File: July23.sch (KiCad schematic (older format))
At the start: 42 parts, among them P1 12v In, P2 HeatOut, P3 LED, P4 Temp1, P5 Temp2, P6 Temp3, P7 ExtPwr, Q16 Q_NMOS_GSD, Q17 Q_NMOS_GSD, U1 Teensy_3.1, U2 LM358, U3 CD74HC4067, U4 MC78M05CDT, U5 NCR405U

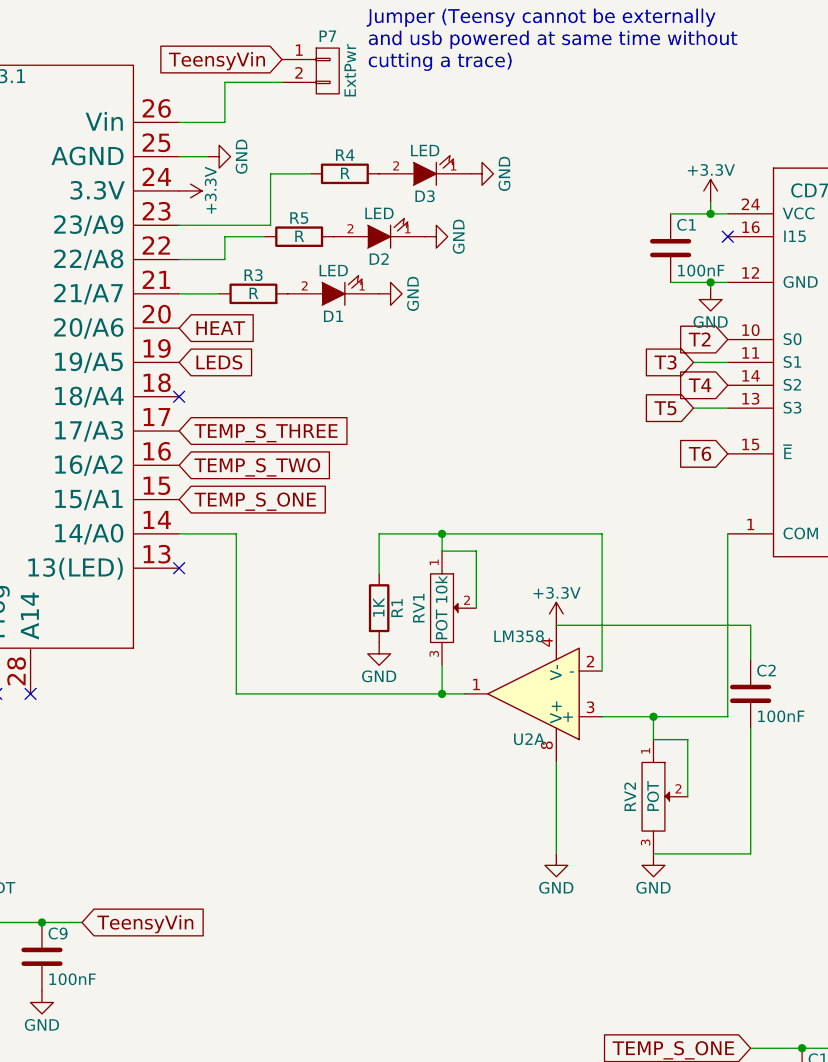
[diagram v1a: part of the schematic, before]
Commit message: OpAmp circuit needs checking
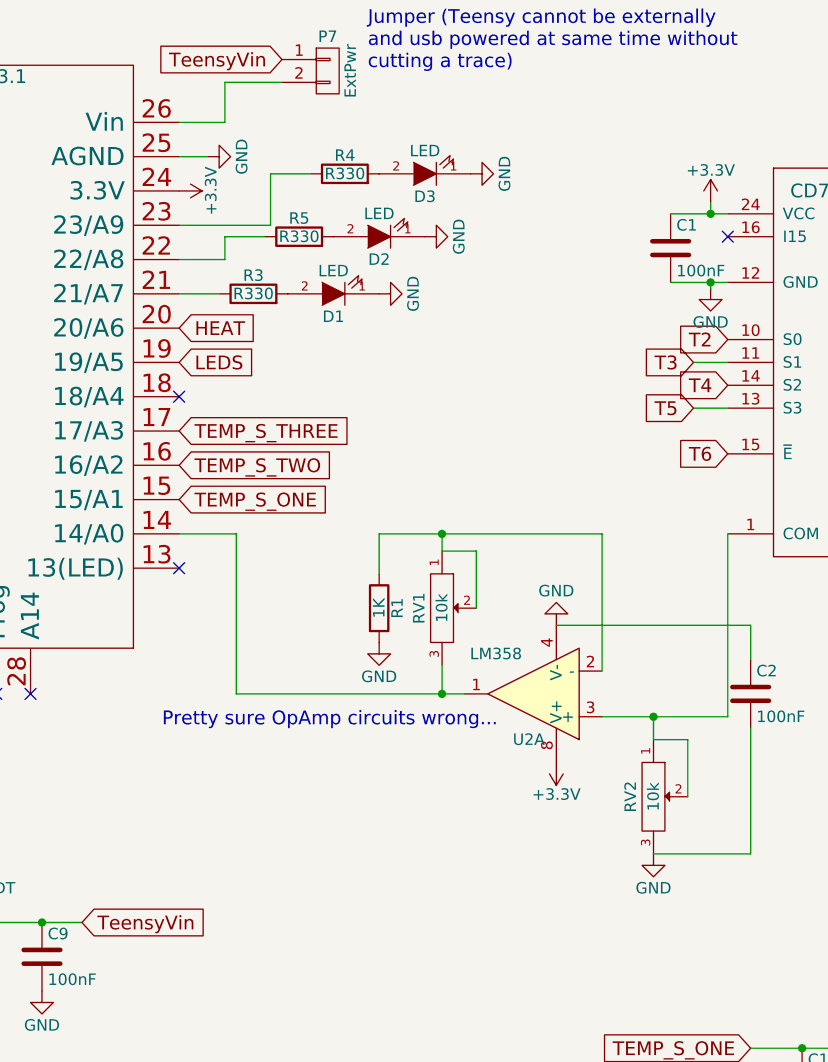
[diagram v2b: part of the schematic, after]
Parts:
- R3, R4, R5: value R -> R330
- RV1: value POT 10k -> 10k
- RV2: value POT -> 10k
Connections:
- net +3V3: now also U2.8 (V+); no longer C2.1, U2.4 (V-)
- net GND: now also C2.1, U2.4 (V-); no longer U2.8 (V+)
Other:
- note added: "Pretty sure OpAmp circuits wrong..."
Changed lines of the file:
@@
 P 4575 3650
 F 0 "U2" H 4525 3850 50  0000 L CNN
-F 1 "LM358" H 4525 3400 50  0000 L CNN
+F 1 "LM358" H 4625 3475 50  0000 L CNN
 F 2 "Housings_DIP:DIP-8_W7.62mm" H 4575 3650 50  0001 C CNN
 F 3 "" H 4575 3650 50  0000 C CNN
@@
 P 5100 4100
 F 0 "RV2" H 5100 4000 50  0000 C CNN
-F 1 "POT" H 5100 4100 50  0000 C CNN
+F 1 "10k" H 5100 4100 50  0000 C CNN
 F 2 "Potentiometers:Potentiometer_Trimmer-Suntan-TSR-3386P" H 5100 4100 50  0001 C CNN
 F 3 "" H 5100 4100 50  0000 C CNN
@@
 P 4175 3275
 F 0 "RV1" H 4175 3175 50  0000 C CNN
-F 1 "POT 10k" H 4175 3275 50  0000 C CNN
+F 1 "10k" H 4175 3275 50  0000 C CNN
 F 2 "Potentiometers:Potentiometer_Trimmer-Suntan-TSR-3386P" H 4175 3275 50  0001 C CNN
 F 3 "" H 4175 3275 50  0000 C CNN
@@
 L +3.3V #PWR08
 U 1 1 56C888B3
-P 4675 3350
-F 0 "#PWR08" H 4675 3200 50  0001 C CNN
-F 1 "+3.3V" H 4675 3490 50  0000 C CNN
-F 2 "" H 4675 3350 50  0000 C CNN
-F 3 "" H 4675 3350 50  0000 C CNN
-	1    4675 3350
-	1    0    0    -1
+P 4675 3950
+F 0 "#PWR08" H 4675 3800 50  0001 C CNN
+F 1 "+3.3V" H 4675 4090 50  0000 C CNN
+F 2 "" H 4675 3950 50  0000 C CNN
+F 3 "" H 4675 3950 50  0000 C CNN
+	1    4675 3950
+	-1   0    0    1
 $EndComp
 $Comp
@@
 P 3350 1900
 F 0 "R3" V 3430 1900 50  0000 C CNN
-F 1 "R" V 3350 1900 50  0000 C CNN
+F 1 "R330" V 3350 1900 50  0000 C CNN
 F 2 "Resistors_SMD:R_0805_HandSoldering" V 3280 1900 50  0001 C CNN
 F 3 "" H 3350 1900 50  0000 C CNN
@@
 P 3750 1375
 F 0 "R4" V 3830 1375 50  0000 C CNN
-F 1 "R" V 3750 1375 50  0000 C CNN
+F 1 "R330" V 3750 1375 50  0000 C CNN
 F 2 "Resistors_SMD:R_0805_HandSoldering" V 3680 1375 50  0001 C CNN
 F 3 "" H 3750 1375 50  0000 C CNN
@@
 P 3550 1650
 F 0 "R5" V 3630 1650 50  0000 C CNN
-F 1 "R" V 3550 1650 50  0000 C CNN
+F 1 "R330" V 3550 1650 50  0000 C CNN
 F 2 "Resistors_SMD:R_0805_HandSoldering" V 3480 1650 50  0001 C CNN
 F 3 "" H 3550 1650 50  0000 C CNN
@@
 L GND #PWR015
 U 1 1 56E2450E
-P 4675 4350
-F 0 "#PWR015" H 4675 4100 50  0001 C CNN
-F 1 "GND" H 4675 4200 50  0000 C CNN
-F 2 "" H 4675 4350 50  0000 C CNN
-F 3 "" H 4675 4350 50  0000 C CNN
-	1    4675 4350
-	1    0    0    -1
+P 4675 3350
+F 0 "#PWR015" H 4675 3100 50  0001 C CNN
+F 1 "GND" H 4675 3200 50  0000 C CNN
+F 2 "" H 4675 3350 50  0000 C CNN
+F 3 "" H 4675 3350 50  0000 C CNN
+	1    4675 3350
+	-1   0    0    1
 $EndComp
 $Comp
@@
 	5100 3850 5250 3850
 Wire Wire Line
-	4675 4350 4675 3950
-Wire Wire Line
 	4175 3025 4325 3025
 Wire Wire Line
@@
 	1200 4375 1200 4650
 Connection ~ 1200 4650
+Text Notes 2950 3800 0    60   ~ 0
+Pretty sure OpAmp circuits wrong...
 $EndSCHEMATC

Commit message: opamp flipped for clarity
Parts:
- RV1, RV2: symbol POT -> POT-RESCUE-July23
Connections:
- net labels added: Amp+, Amp-, Amp_Out
- wire segments 96 -> 94
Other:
- note removed: "Pretty sure OpAmp circuits wrong..."
- moved on the sheet: C2, R1
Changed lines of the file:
@@
 EESchema Schematic File Version 2
+LIBS:July23-rescue
 LIBS:power
 LIBS:device
@@
 F 3 "" H 4575 3650 50  0000 C CNN
 	1    4575 3650
-	-1   0    0    1
-$EndComp
-$Comp
-L POT RV2
+	-1   0    0    -1
+$EndComp
+$Comp
+L POT-RESCUE-July23 RV2
 U 1 1 56B985A4
-P 5100 4100
-F 0 "RV2" H 5100 4000 50  0000 C CNN
-F 1 "10k" H 5100 4100 50  0000 C CNN
-F 2 "Potentiometers:Potentiometer_Trimmer-Suntan-TSR-3386P" H 5100 4100 50  0001 C CNN
-F 3 "" H 5100 4100 50  0000 C CNN
-	1    5100 4100
+P 5425 4100
+F 0 "RV2" H 5425 4000 50  0000 C CNN
+F 1 "10k" H 5425 4100 50  0000 C CNN
+F 2 "Potentiometers:Potentiometer_Trimmer-Suntan-TSR-3386P" H 5425 4100 50  0001 C CNN
+F 3 "" H 5425 4100 50  0000 C CNN
+	1    5425 4100
 	0    1    1    0
 $EndComp
 $Comp
-L POT RV1
+L POT-RESCUE-July23 RV1
 U 1 1 56B99053
-P 4175 3275
-F 0 "RV1" H 4175 3175 50  0000 C CNN
-F 1 "10k" H 4175 3275 50  0000 C CNN
-F 2 "Potentiometers:Potentiometer_Trimmer-Suntan-TSR-3386P" H 4175 3275 50  0001 C CNN
-F 3 "" H 4175 3275 50  0000 C CNN
-	1    4175 3275
-	0    1    1    0
+P 4175 4025
+F 0 "RV1" H 4175 3925 50  0000 C CNN
+F 1 "10k" H 4175 4025 50  0000 C CNN
+F 2 "Potentiometers:Potentiometer_Trimmer-Suntan-TSR-3386P" H 4175 4025 50  0001 C CNN
+F 3 "" H 4175 4025 50  0000 C CNN
+	1    4175 4025
+	0    1    -1   0
 $EndComp
 $Comp
 L R R1
 U 1 1 56B99A73
-P 3900 3275
-F 0 "R1" V 3980 3275 50  0000 C CNN
-F 1 "1K" V 3900 3275 50  0000 C CNN
-F 2 "Resistors_SMD:R_0805_HandSoldering" V 3830 3275 50  0001 C CNN
-F 3 "" H 3900 3275 50  0000 C CNN
-	1    3900 3275
+P 4175 4575
+F 0 "R1" V 4255 4575 50  0000 C CNN
+F 1 "1K" V 4175 4575 50  0000 C CNN
+F 2 "Resistors_SMD:R_0805_HandSoldering" V 4105 4575 50  0001 C CNN
+F 3 "" H 4175 4575 50  0000 C CNN
+	1    4175 4575
 	1    0    0    -1
 $EndComp
@@
 L C C2
 U 1 1 56B9C865
-P 5525 3650
-F 0 "C2" H 5550 3750 50  0000 L CNN
-F 1 "100nF" H 5550 3550 50  0000 L CNN
-F 2 "Capacitors_SMD:C_0805_HandSoldering" H 5563 3500 50  0001 C CNN
-F 3 "" H 5525 3650 50  0000 C CNN
-	1    5525 3650
-	1    0    0    -1
+P 4175 3225
+F 0 "C2" H 4200 3325 50  0000 L CNN
+F 1 "100nF" H 4200 3125 50  0000 L CNN
+F 2 "Capacitors_SMD:C_0805_HandSoldering" H 4213 3075 50  0001 C CNN
+F 3 "" H 4175 3225 50  0000 C CNN
+	1    4175 3225
+	-1   0    0    1
 $EndComp
 $Comp
@@
 L +3.3V #PWR08
 U 1 1 56C888B3
-P 4675 3950
-F 0 "#PWR08" H 4675 3800 50  0001 C CNN
-F 1 "+3.3V" H 4675 4090 50  0000 C CNN
-F 2 "" H 4675 3950 50  0000 C CNN
-F 3 "" H 4675 3950 50  0000 C CNN
-	1    4675 3950
-	-1   0    0    1
+P 4675 3000
+F 0 "#PWR08" H 4675 2850 50  0001 C CNN
+F 1 "+3.3V" H 4675 3140 50  0000 C CNN
+F 2 "" H 4675 3000 50  0000 C CNN
+F 3 "" H 4675 3000 50  0000 C CNN
+	1    4675 3000
+	-1   0    0    -1
 $EndComp
 $Comp
@@
 L GND #PWR015
 U 1 1 56E2450E
-P 4675 3350
-F 0 "#PWR015" H 4675 3100 50  0001 C CNN
-F 1 "GND" H 4675 3200 50  0000 C CNN
-F 2 "" H 4675 3350 50  0000 C CNN
-F 3 "" H 4675 3350 50  0000 C CNN
-	1    4675 3350
-	-1   0    0    1
+P 4675 3950
+F 0 "#PWR015" H 4675 3700 50  0001 C CNN
+F 1 "GND" H 4675 3800 50  0000 C CNN
+F 2 "" H 4675 3950 50  0000 C CNN
+F 3 "" H 4675 3950 50  0000 C CNN
+	1    4675 3950
+	-1   0    0    -1
 $EndComp
 $Comp
 L GND #PWR016
 U 1 1 56E246E4
-P 5100 4350
-F 0 "#PWR016" H 5100 4100 50  0001 C CNN
-F 1 "GND" H 5100 4200 50  0000 C CNN
-F 2 "" H 5100 4350 50  0000 C CNN
-F 3 "" H 5100 4350 50  0000 C CNN
-	1    5100 4350
+P 5425 4350
+F 0 "#PWR016" H 5425 4100 50  0001 C CNN
+F 1 "GND" H 5425 4200 50  0000 C CNN
+F 2 "" H 5425 4350 50  0000 C CNN
+F 3 "" H 5425 4350 50  0000 C CNN
+	1    5425 4350
 	1    0    0    -1
 $EndComp
@@
 L GND #PWR018
 U 1 1 56E24F5B
-P 3900 3425
-F 0 "#PWR018" H 3900 3175 50  0001 C CNN
-F 1 "GND" H 3900 3275 50  0000 C CNN
-F 2 "" H 3900 3425 50  0000 C CNN
-F 3 "" H 3900 3425 50  0000 C CNN
-	1    3900 3425
+P 4175 4725
+F 0 "#PWR018" H 4175 4475 50  0001 C CNN
+F 1 "GND" H 4175 4575 50  0000 C CNN
+F 2 "" H 4175 4725 50  0000 C CNN
+F 3 "" H 4175 4725 50  0000 C CNN
+	1    4175 4725
 	1    0    0    -1
 $EndComp
@@
 	1    0    0    -1
 $EndComp
+Text Label 4900 3550 0    60   ~ 0
+Amp+
+Text Label 4900 3750 0    60   ~ 0
+Amp-
 Wire Wire Line
 	6600 1375 8325 1375
@@
 	6675 3000 6525 3000
 Wire Wire Line
-	4875 3750 5425 3750
-Wire Wire Line
-	5100 3850 5100 3750
-Connection ~ 5100 3750
-Wire Wire Line
-	5100 3850 5250 3850
-Wire Wire Line
-	4175 3025 4325 3025
-Wire Wire Line
-	4325 3025 4325 3275
-Wire Wire Line
-	4175 3025 4175 2950
-Wire Wire Line
-	3900 2950 4875 2950
-Wire Wire Line
-	4875 2950 4875 3550
-Wire Wire Line
-	4175 3525 4175 3650
+	5425 2950 5425 3850
+Wire Wire Line
+	4175 4350 4950 4350
 Wire Wire Line
 	3275 3650 4275 3650
 Wire Wire Line
-	5425 3750 5425 2950
-Wire Wire Line
-	5250 3850 5250 4100
-Wire Wire Line
-	3900 2950 3900 3125
-Connection ~ 4175 2950
-Connection ~ 4175 3650
-Wire Wire Line
 	5425 2400 5275 2400
 Wire Wire Line
@@
 	5175 1550 5425 1550
 Wire Wire Line
-	5425 1850 5175 1850
-Wire Wire Line
-	5525 3500 5525 3350
-Wire Wire Line
-	5525 3350 4675 3350
-Wire Wire Line
-	5525 3800 5525 4350
-Wire Wire Line
-	5525 4350 5100 4350
+	5175 1850 5425 1850
 Wire Wire Line
 	775  5925 1925 5925
@@
 	1200 4375 1200 4650
 Connection ~ 1200 4650
-Text Notes 2950 3800 0    60   ~ 0
-Pretty sure OpAmp circuits wrong...
+Wire Wire Line
+	4175 4275 4175 4425
+Wire Wire Line
+	4325 4025 4325 4300
+Connection ~ 4175 4350
+Wire Wire Line
+	4325 4300 4175 4300
+Connection ~ 4175 4300
+Wire Wire Line
+	4175 3775 4175 3650
+Connection ~ 4175 3650
+$Comp
+L GND #PWR?
+U 1 1 5797FF63
+P 4175 3375
+F 0 "#PWR?" H 4175 3125 50  0001 C CNN
+F 1 "GND" H 4175 3225 50  0000 C CNN
+F 2 "" H 4175 3375 50  0000 C CNN
+F 3 "" H 4175 3375 50  0000 C CNN
+	1    4175 3375
+	-1   0    0    -1
+$EndComp
+Wire Wire Line
+	4675 3000 4675 3350
+Wire Wire Line
+	4175 3075 4675 3075
+Connection ~ 4675 3075
+Wire Wire Line
+	5575 4100 5600 4100
+Wire Wire Line
+	5600 4100 5600 3825
+Wire Wire Line
+	5600 3825 5425 3825
+Connection ~ 5425 3825
+Wire Wire Line
+	4875 3550 5425 3550
+Connection ~ 5425 3550
+Wire Wire Line
+	4950 4350 4950 3750
+Wire Wire Line
+	4950 3750 4875 3750
+Text Label 3700 3650 0    60   ~ 0
+Amp_Out
 $EndSCHEMATC

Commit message: fixing up opamp on PCB (work in progress)
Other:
- note added: "TODO: Check grounding of fills"
- note added: "Teensy can supply us 3v3?"
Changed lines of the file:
@@
 F 3 "" H 4175 3225 50  0000 C CNN
 	1    4175 3225
-	-1   0    0    1
+	-1   0    0    -1
 $EndComp
 $Comp
@@
 Connection ~ 4175 3650
 $Comp
-L GND #PWR?
+L GND #PWR038
 U 1 1 5797FF63
 P 4175 3375
-F 0 "#PWR?" H 4175 3125 50  0001 C CNN
+F 0 "#PWR038" H 4175 3125 50  0001 C CNN
 F 1 "GND" H 4175 3225 50  0000 C CNN
 F 2 "" H 4175 3375 50  0000 C CNN
@@
 Text Label 3700 3650 0    60   ~ 0
 Amp_Out
+Text Notes 3600 2300 0    60   ~ 0
+Teensy can supply us 3v3?
+Text Notes 5850 3750 0    60   ~ 0
+TODO: Check grounding of fills
 $EndSCHEMATC
